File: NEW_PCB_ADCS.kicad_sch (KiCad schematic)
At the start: 14 parts, among them J3 AUX, J4 SWD, U10 LDL1117S33R

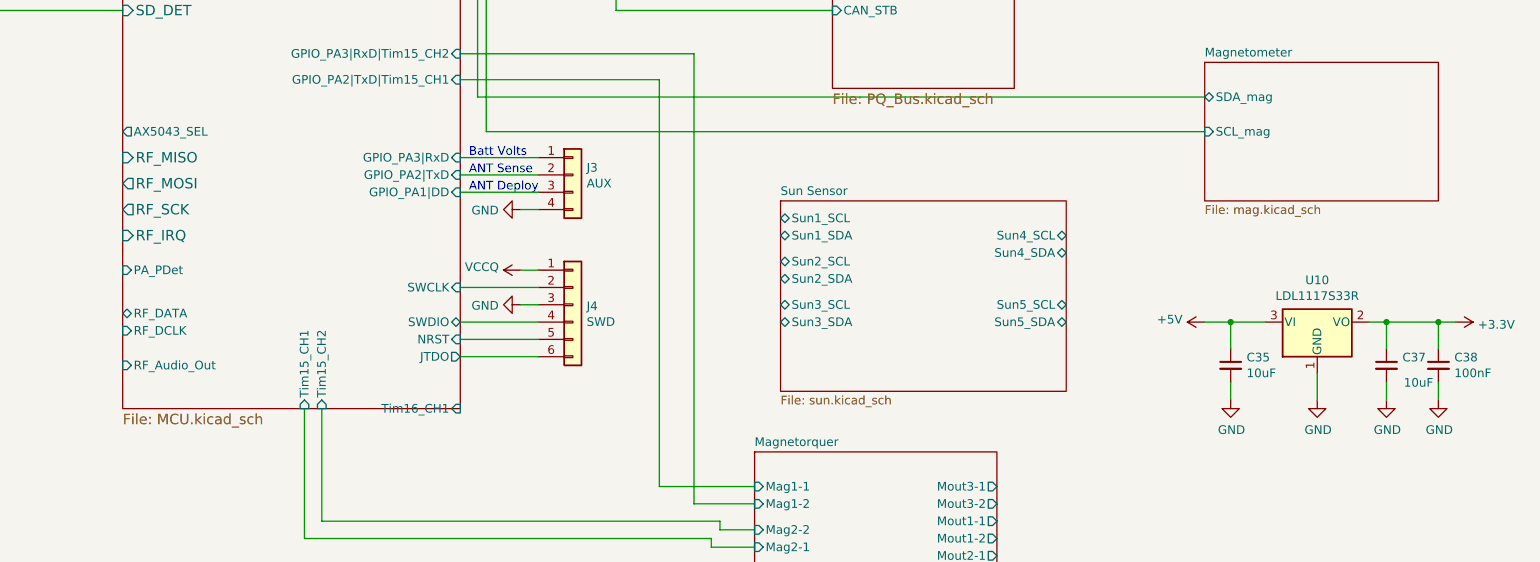
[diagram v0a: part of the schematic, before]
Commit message: Clean-up schematic
Closes #4
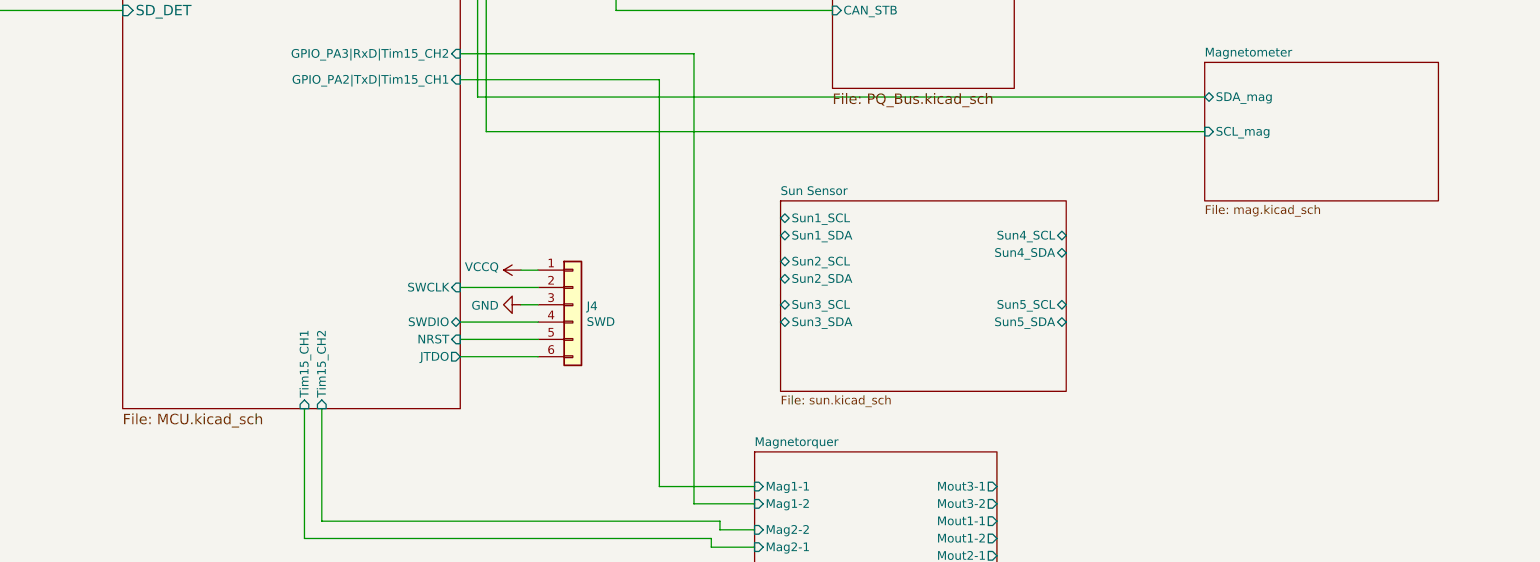
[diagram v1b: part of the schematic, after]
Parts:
- removed C35, C37: 10uF, Capacitor_SMD:C_0603_1608Metric_Pad1.08x0.95mm_HandSolder, symbol Device:C_Small
- removed C38: 100nF, Capacitor_SMD:C_0603_1608Metric, symbol Device:C_Small
- removed J3: AUX, Connector_Molex:Molex_PicoBlade_53261-0471_1x04-1MP_P1.25mm_Horizontal, symbol Connector_Generic:Conn_01x04
- removed U10: LDL1117S33R, Package_TO_SOT_SMD:SOT-223-3_TabPin2, symbol Regulator_Linear:LM1117-3.3
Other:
- sheet MCU ports: added none; removed AX5043_SEL, GPIO_PA1|DD, GPIO_PA2|TxD, GPIO_PA3|RxD, PA_PDet, RF_Audio_Out, RF_DATA, RF_DCLK, RF_IRQ, RF_MISO, RF_MOSI, RF_SCK, Tim16_CH1
- note removed: "ANT Deploy"
- note removed: "ANT Sense"
- note removed: "Batt Volts"

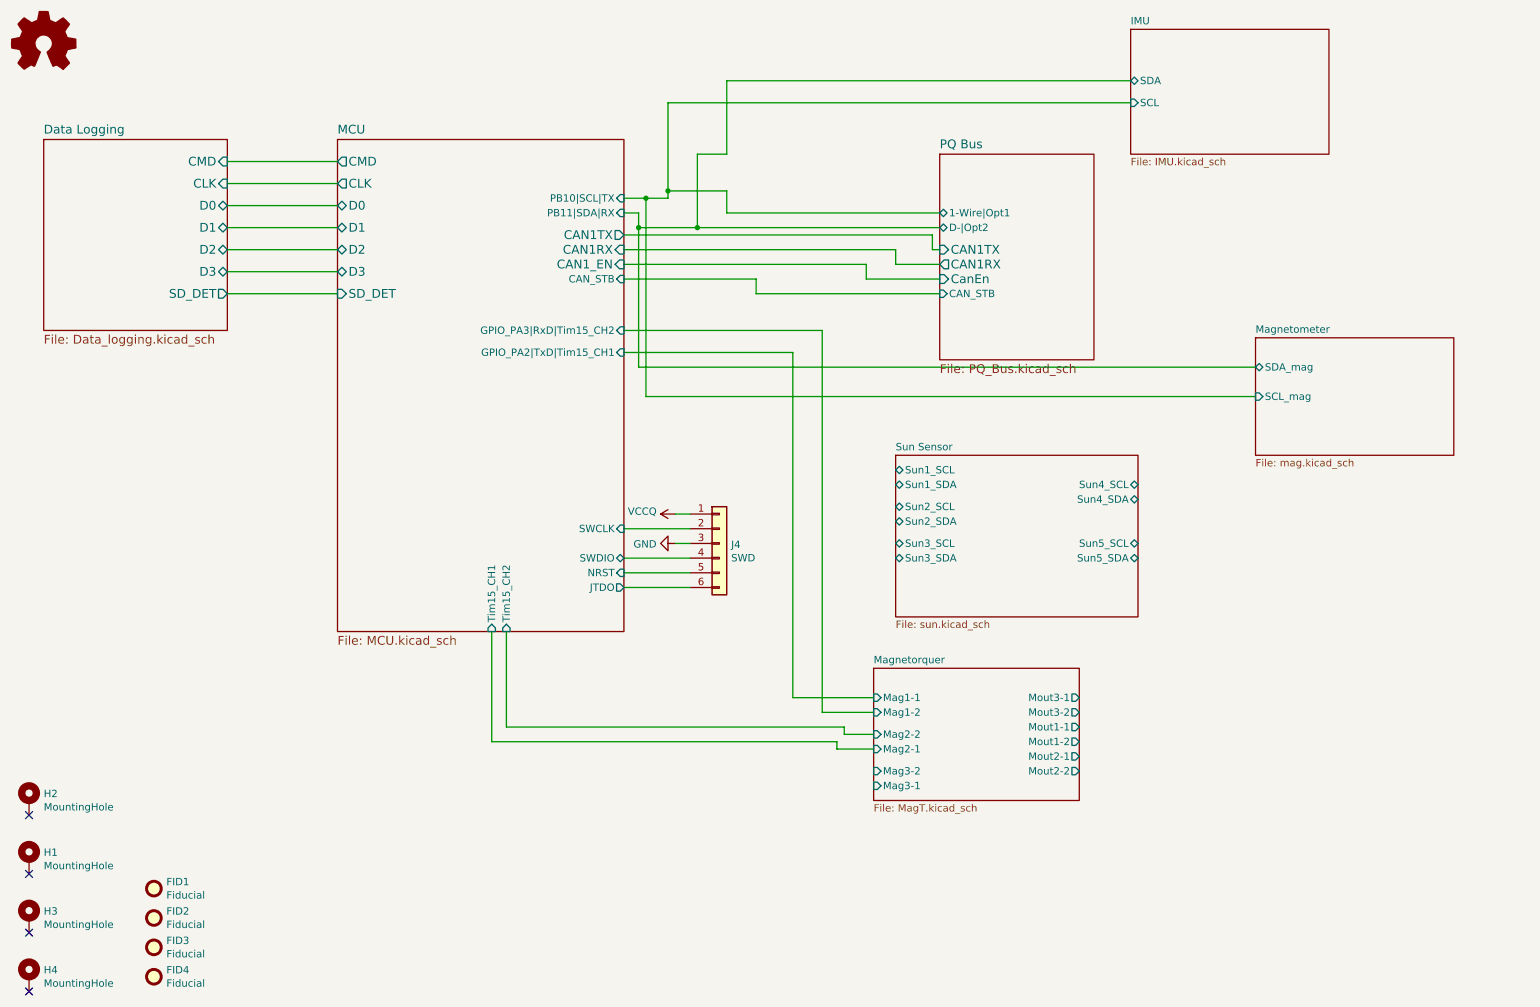
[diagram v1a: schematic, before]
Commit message: Add I2C multiplexer
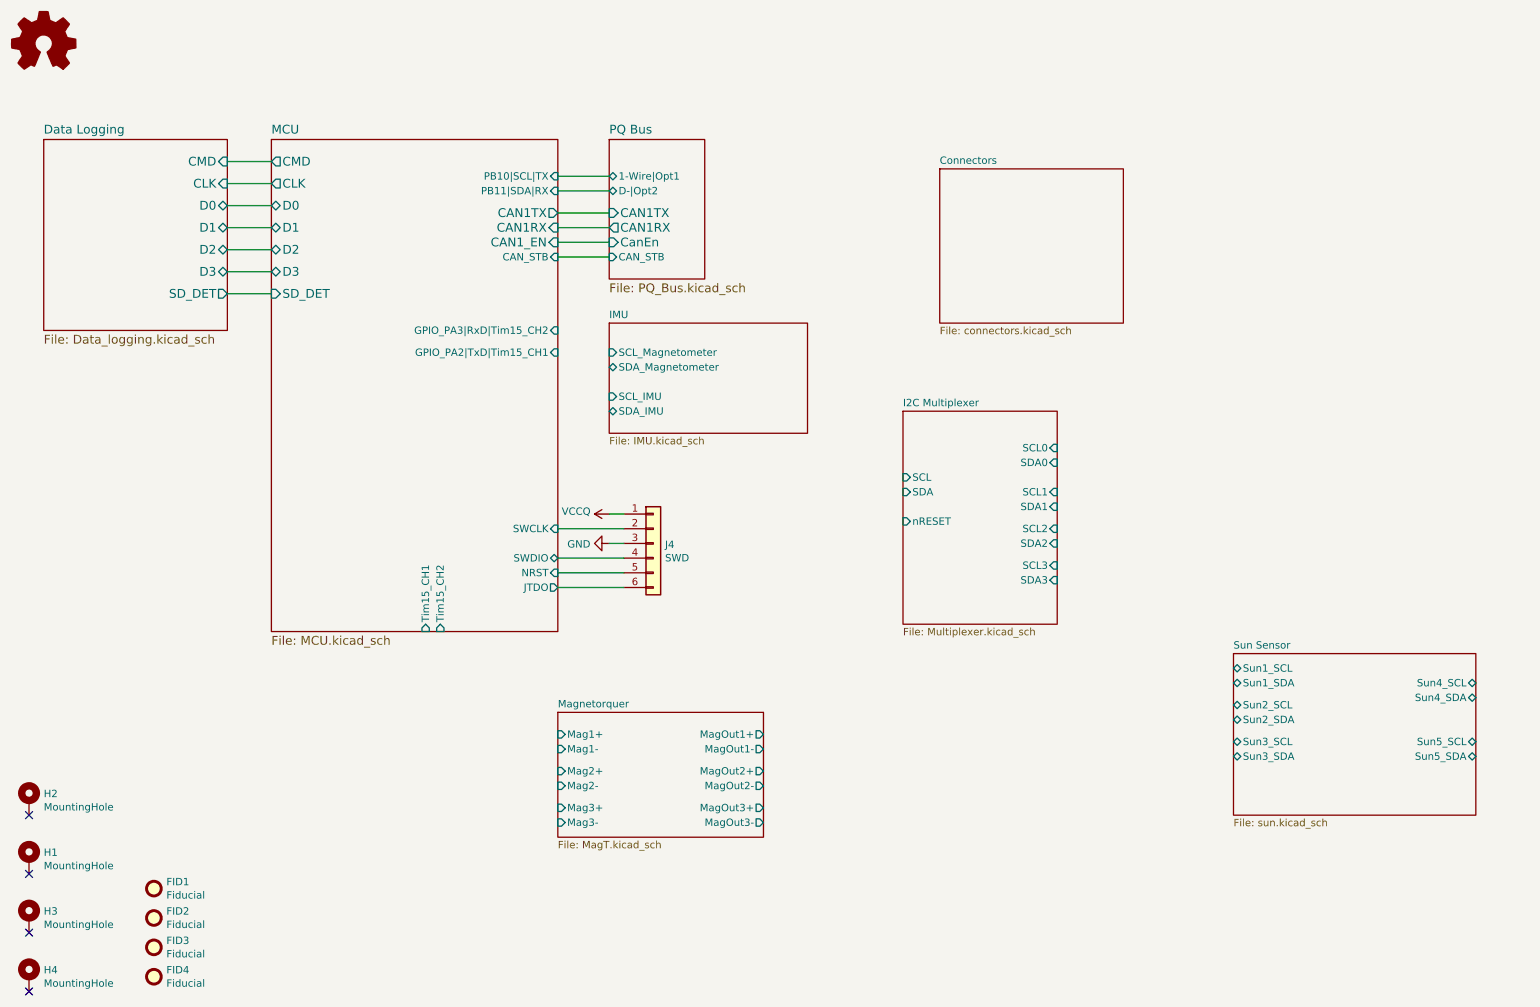
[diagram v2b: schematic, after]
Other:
- removed sheet Magnetometer
- added sheet Connectors (connectors.kicad_sch)
- added sheet I2C Multiplexer (Multiplexer.kicad_sch)
- sheet IMU ports: added SCL_IMU, SCL_Magnetometer, SDA_IMU, SDA_Magnetometer; removed SCL, SDA
- sheet Magnetorquer ports: added Mag1+, Mag1-, Mag2+, Mag2-, Mag3+, Mag3-, MagOut1+, MagOut1-, MagOut2+, MagOut2-, MagOut3+, MagOut3-; removed Mag1-1, Mag1-2, Mag2-1, Mag2-2, Mag3-1, Mag3-2, Mout1-1, Mout1-2, Mout2-1, Mout2-2, Mout3-1, Mout3-2
- moved on the sheet: J4

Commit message: Add connections between existing sheets
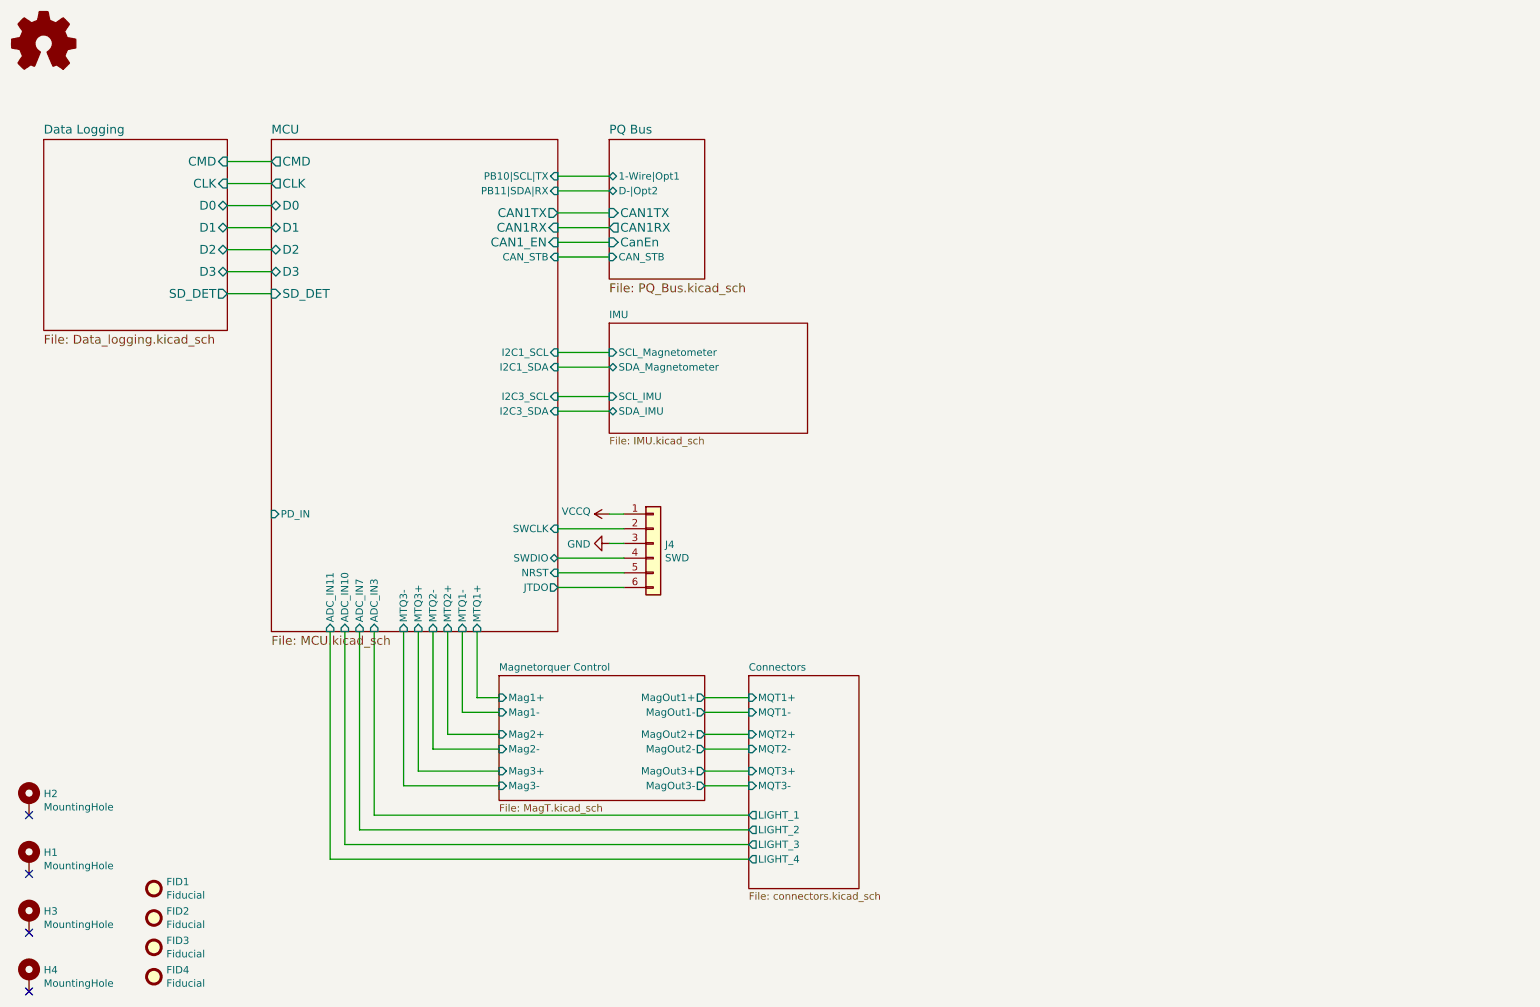
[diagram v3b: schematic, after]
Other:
- sheet Magnetorquer renamed Magnetorquer Control
- removed sheet I2C Multiplexer
- removed sheet Sun Sensor
- sheet Connectors ports: added LIGHT_1, LIGHT_2, LIGHT_3, LIGHT_4, MQT1+, MQT1-, MQT2+, MQT2-, MQT3+, MQT3-; removed none
- sheet MCU ports: added ADC_IN10, ADC_IN11, ADC_IN3, ADC_IN7, I2C1_SCL, I2C1_SDA, I2C3_SCL, I2C3_SDA, MTQ1+, MTQ1-, MTQ2+, MTQ2-, MTQ3+, MTQ3-, PD_IN; removed GPIO_PA2|TxD|Tim15_CH1, GPIO_PA3|RxD|Tim15_CH2, Tim15_CH1, Tim15_CH2

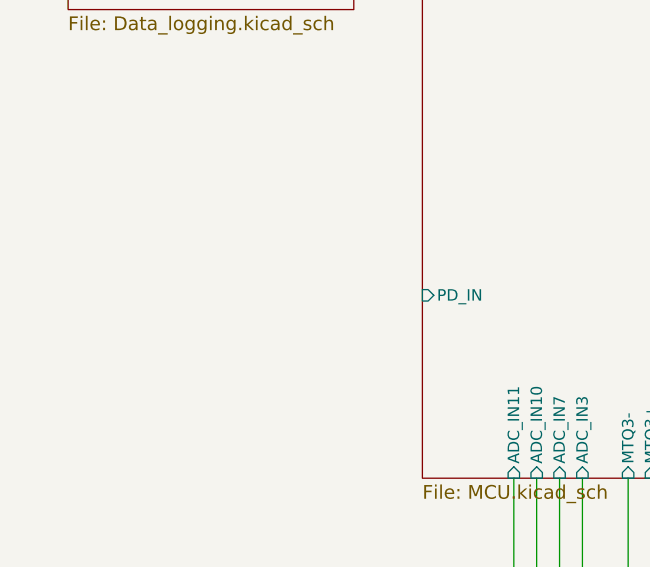
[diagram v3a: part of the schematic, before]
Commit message: Add PD circuit
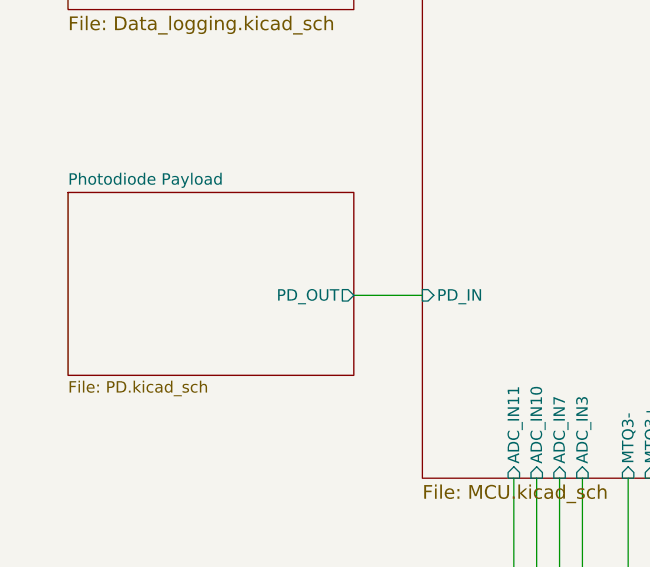
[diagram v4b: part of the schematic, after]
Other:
- added sheet Photodiode Payload (PD.kicad_sch)
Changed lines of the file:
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@@
+    (stroke (width 0) (type default))
+  )
+  (wire (pts (xy 55.88 104.14) (xy 63.5 104.14))
     (stroke (width 0) (type default))
   )
@@
       )
     )
+  )
+  (sheet (at 24.13 92.71) (size 31.75 20.32) (fields_autoplaced)
+    (stroke (width 0.1524) (type solid))
+    (fill (color 0 0 0 0.0000))
+    (property "Sheetname" "Photodiode Payload" (at 24.13 91.9984 0)
+      (effects (font (size 1.27 1.27)) (justify left bottom))
+    )
+    (property "Sheetfile" "PD.kicad_sch" (at 24.13 113.6146 0)
+      (effects (font (size 1.27 1.27)) (justify left top))
+    )
+    (pin "PD_OUT" output (at 55.88 104.14 0)
+      (effects (font (size 1.27 1.27)) (justify right))
+    )
+    (instances
+      (project "NEW_PCB_ADCS"
+        (path "/42c40d7d-71af-4ce9-bac9-d638f259c957" (page "8"))
+      )
+    )
